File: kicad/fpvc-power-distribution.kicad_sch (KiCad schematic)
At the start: 0 parts

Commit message: feat: Plan mosfet based solenoid and clutch actuation
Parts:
- added D1, D2, D4: 1N5819, Diode_THT:D_DO-41_SOD81_P10.16mm_Horizontal, symbol Diode:1N5819
- added J1, J3: Solenoid1, symbol Connector:Screw_Terminal_01x02
- added J2: PLC-S1, symbol Connector:Screw_Terminal_01x01
- added J4: PLC-S2, symbol Connector:Screw_Terminal_01x01
- added J6: Clutch, symbol Connector:Screw_Terminal_01x02
- added J8: PLC-C, symbol Connector:Screw_Terminal_01x01
- added Q1, Q2, Q4: IRLZ44N, Package_TO_SOT_THT:TO-220-3_Vertical, symbol Transistor_FET:IRLZ44N
- added R1, R3, R6: 220, symbol Device:R
- added R2, R4, R8: 10k, symbol Device:R
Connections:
- new net: D2.1 (K), J3.1 (Pin_1)
- new net: D2.2 (A), J3.2 (Pin_2), Q2.2 (D)
- new net: J2.1 (Pin_1), R1.1
- new net: Q1.1 (G), R1.2, R2.1
- new net: J8.1 (Pin_1), R6.1
- new net: Q4.1 (G), R6.2, R8.1
- new net: D4.2 (A), J6.2 (Pin_2), Q4.2 (D)
- new net: D1.1 (K), J1.1 (Pin_1)
- new net: D1.2 (A), J1.2 (Pin_2), Q1.2 (D)
- new net: Q2.1 (G), R3.2, R4.1
- new net: J4.1 (Pin_1), R3.1
- new net +12V: D4.1 (K), J6.1 (Pin_1)
- new net GND: Q1.3 (S), Q2.3 (S), Q4.3 (S), R2.2, R4.2, R8.2
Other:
- company: (none) -> Aiden Cherniske | Bucknell Mechanical Engineering Department
- title: (none) -> Fluid Power Vehicle Challenge Power Distribution Board

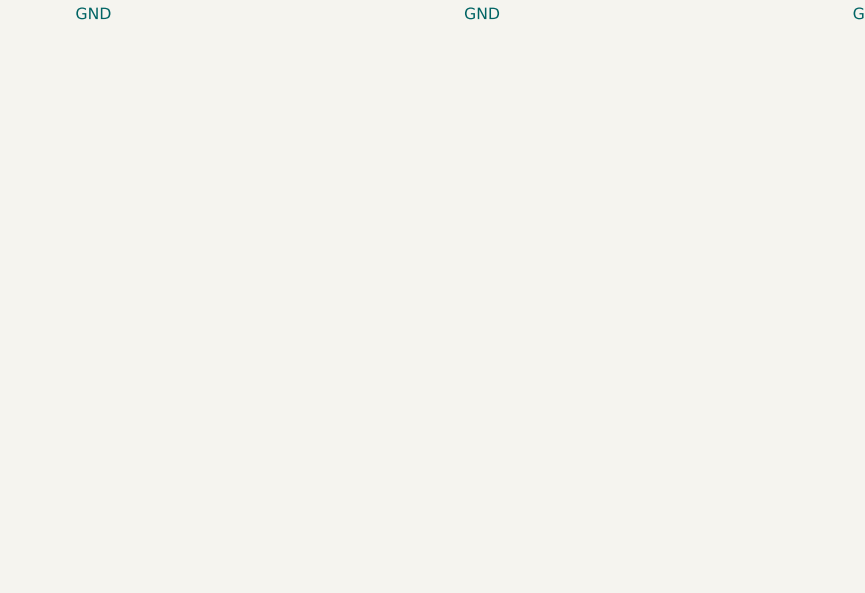
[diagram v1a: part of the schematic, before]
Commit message: feat: Create voltage regulator symbol and schematic
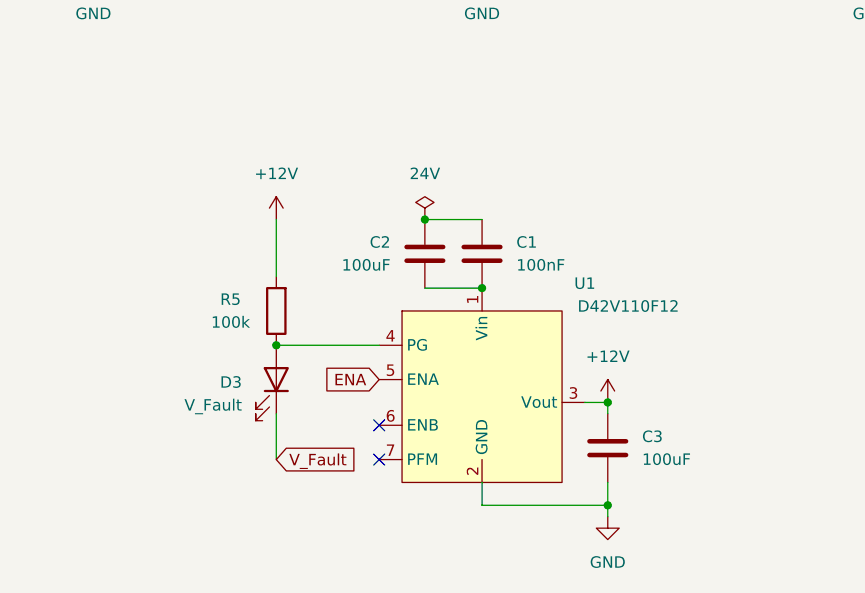
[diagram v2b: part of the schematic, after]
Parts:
- added C1: 100nF, symbol Device:C
- added C2, C3: 100uF, symbol Device:C
- added D3: V_Fault, symbol Device:LED
- added R5: 100k, symbol Device:R
- added U1: D42V110F12, symbol library:D42V110F12
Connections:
- net +12V: now also C3.1, R5.2, U1.3 (Vout)
- net GND: now also C3.2, U1.2 (GND)
- new net: D3.2 (A), R5.1, U1.4 (PG)
- new net: C1.2, C2.2, U1.1 (Vin)
- new net: C1.1, C2.1
- new net ENA: U1.5 (ENA)
- new net V_Fault: D3.1 (K)
- no-connect marks 0 -> 2

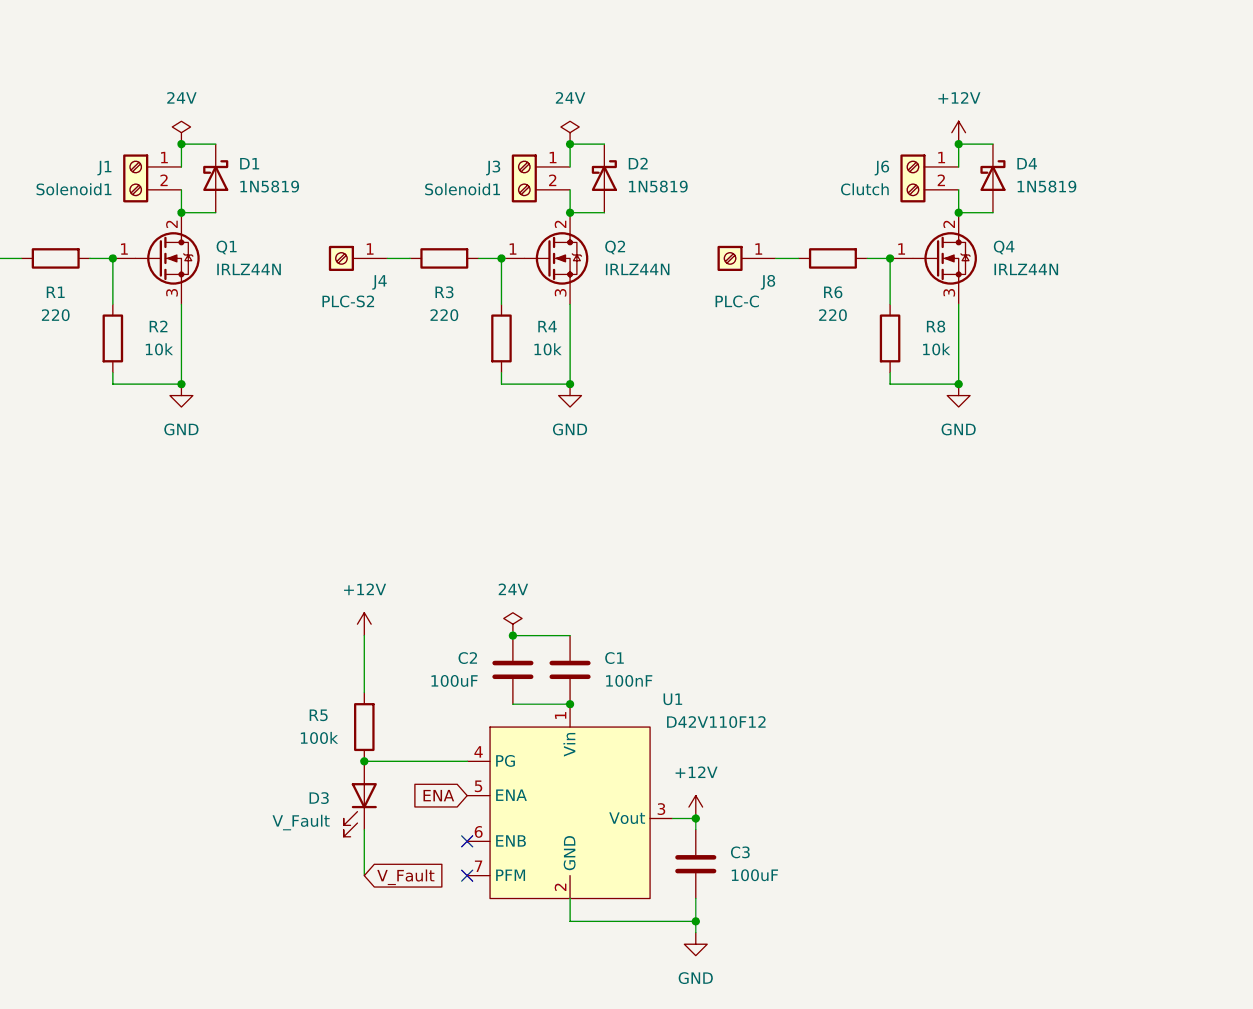
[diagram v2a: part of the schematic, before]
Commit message: feat: Add proper regulator fault detection and power indication
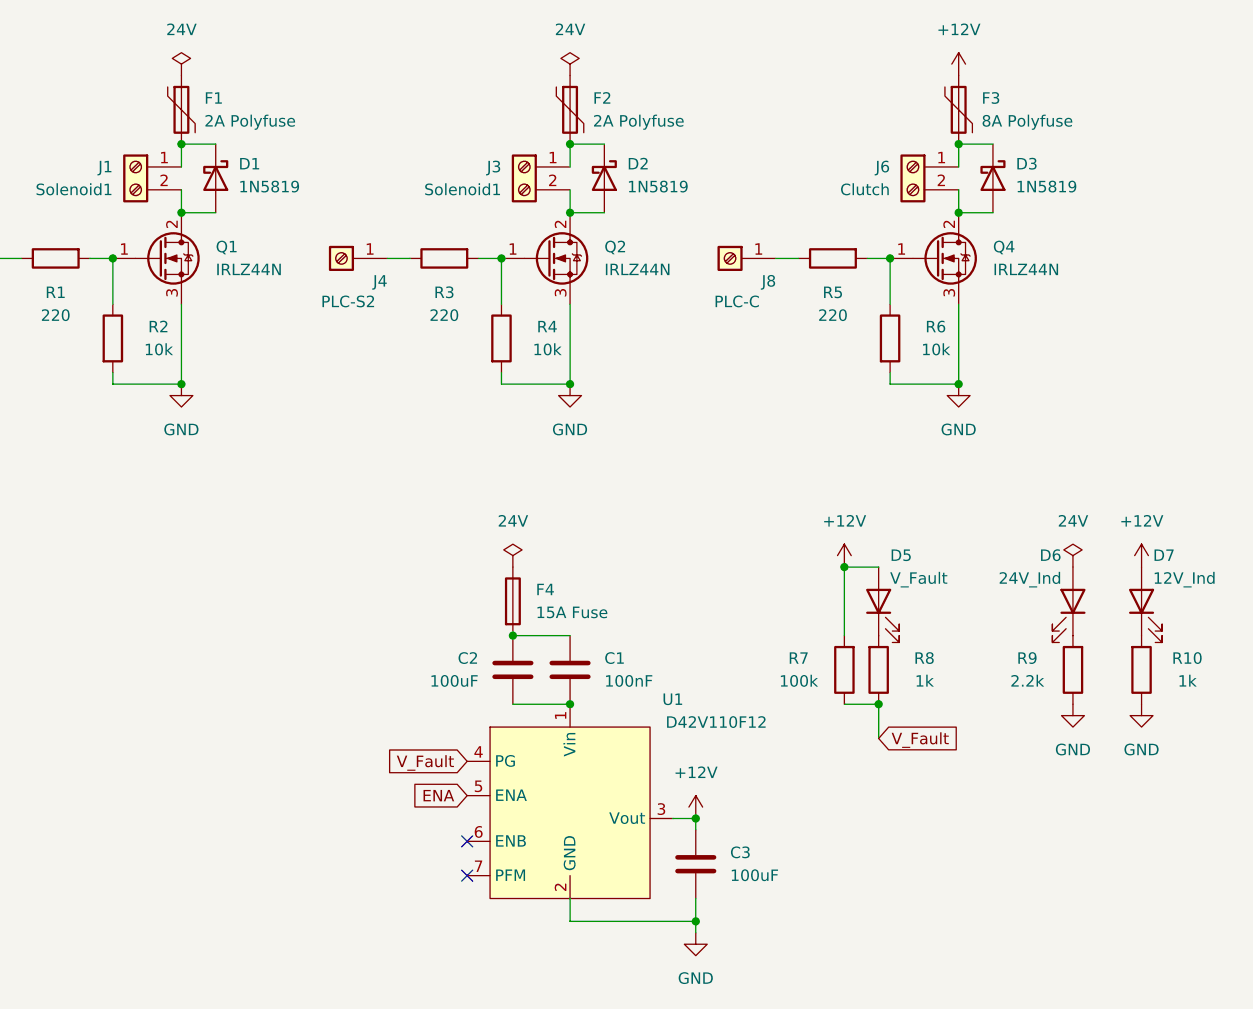
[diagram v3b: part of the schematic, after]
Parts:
- removed D3: V_Fault, symbol Device:LED
- added D5: V_Fault, symbol Device:LED
- added D6: 24V_Ind, symbol Device:LED
- added D7: 12V_Ind, symbol Device:LED
- added F1, F2: 2A Polyfuse, symbol Device:Polyfuse
- added F3: 8A Polyfuse, symbol Device:Polyfuse
- added F4: 15A Fuse, symbol Device:Fuse
- added R10, R8: 1k, symbol Device:R
- added R9: 2.2k, symbol Device:R
- renumbered D4 to D3, R6 to R5, R8 to R6, R5 to R7
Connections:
- net +12V: now also D5.2 (A), D7.2 (A), F3.1; no longer D3.1 (K), J6.1 (Pin_1)
- net GND: now also R10.1, R9.1
- net V_Fault: now also R7.1, U1.4 (PG), R8.1
- net at D2.1 (K), J3.1 (Pin_1): now also F2.2
- net at D1.1 (K), J1.1 (Pin_1): now also F1.2
- net at C1.1, C2.1: now also F4.2
- new net: D6.1 (K), R9.2
- new net: D7.1 (K), R10.2
- new net: D5.1 (K), R8.2
- new net: D3.1 (K), F3.2, J6.1 (Pin_1)
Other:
- moved on the sheet: R7

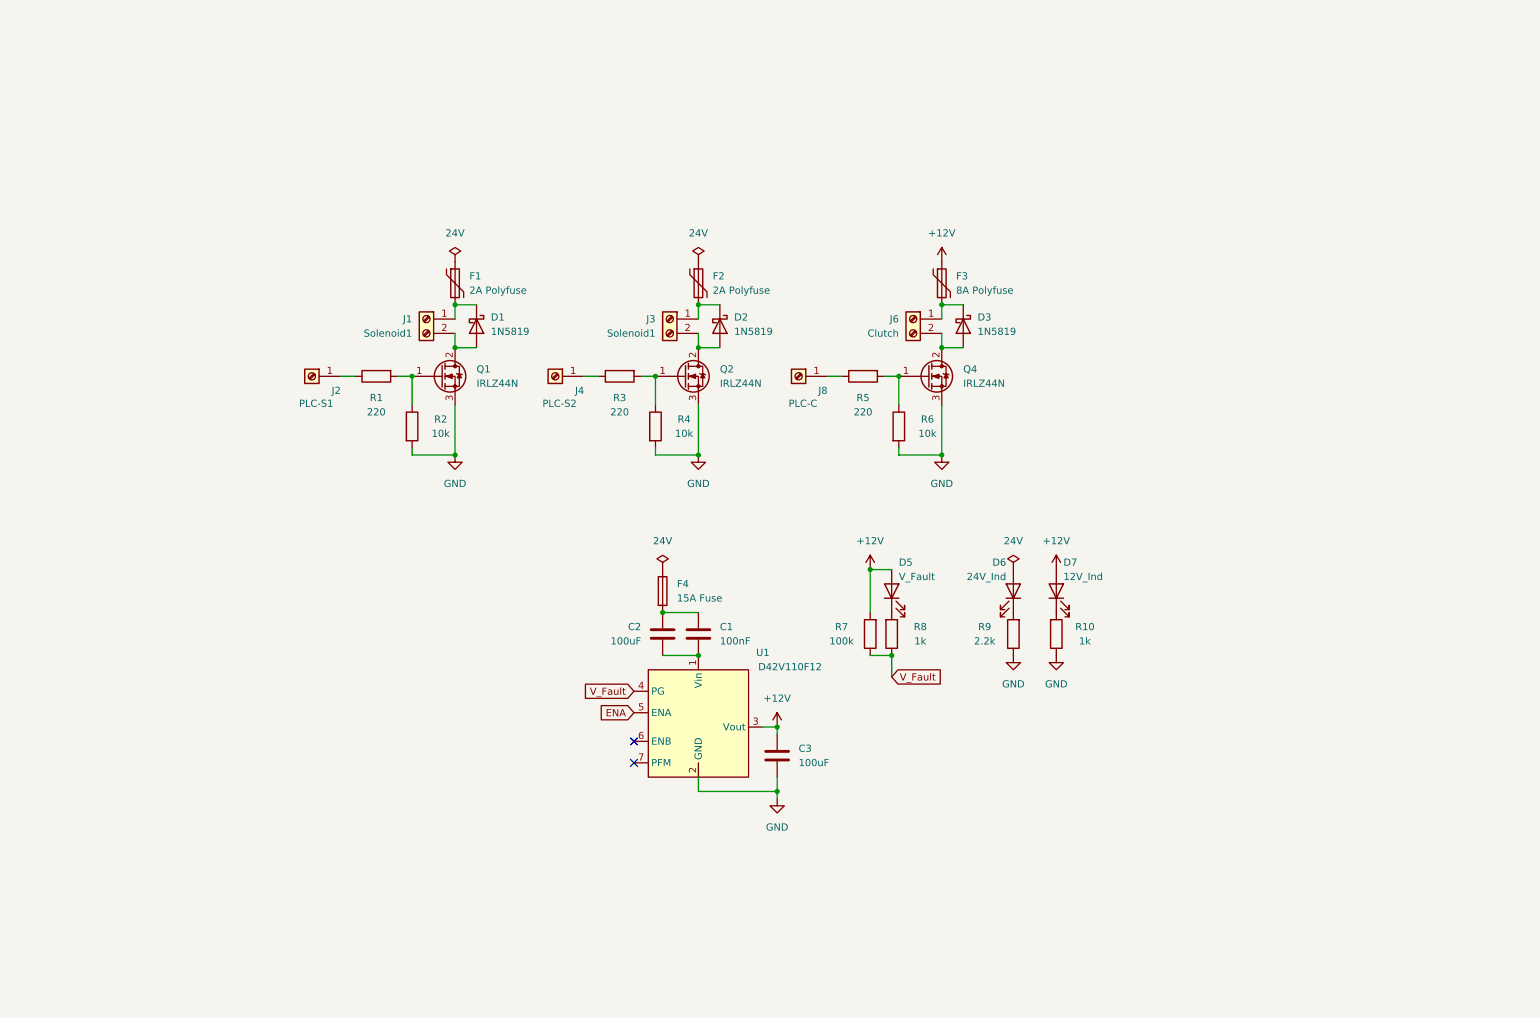
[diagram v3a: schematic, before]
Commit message: feat: Add 5V DC/DC converter for PLC
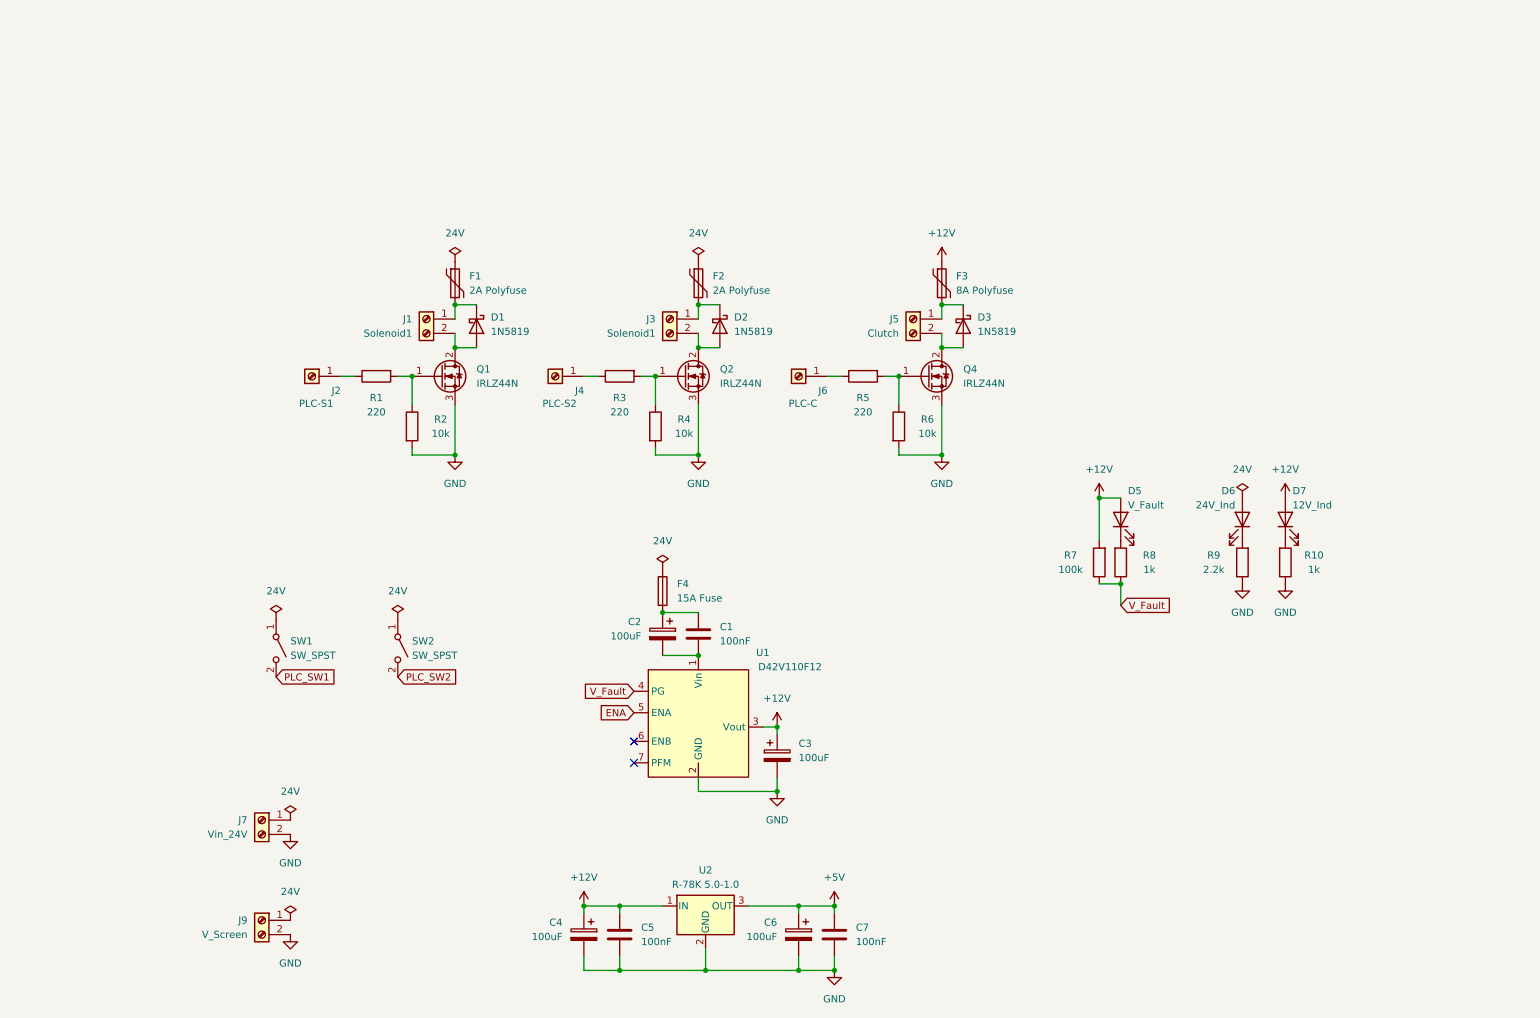
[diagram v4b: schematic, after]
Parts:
- removed C2, C3: 100uF, symbol Device:C
- added C2, C3, C4, C6: 100uF, symbol Device:C_Polarized
- added C5, C7: 100nF, symbol Device:C
- added J7: Vin_24V, symbol Connector:Screw_Terminal_01x02
- added J9: V_Screen, symbol Connector:Screw_Terminal_01x02
- added SW1, SW2: SW_SPST, symbol Switch:SW_SPST
- added U2: R-78K 5.0-1.0, Converter_DCDC:Converter_DCDC_RECOM_R-78E-0.5_THT, symbol Regulator_Switching:R-785.0-1.0
- renumbered J6 to J5, J8 to J6
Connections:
- net +12V: now also C3.1, C4.1, C5.1, U2.1 (IN)
- net GND: now also C3.2, C4.2, C5.2, C6.2, C7.2, J7.2 (Pin_2), J9.2 (Pin_2), U2.2 (GND)
- net at C1.1, F4.2: now also C2.1
- net at C1.2, U1.1 (Vin): now also C2.2
- new net +5V: C6.1, C7.1, U2.3 (OUT)
- new net PLC_SW1: SW1.2 (B)
- new net PLC_SW2: SW2.2 (B)
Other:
- moved on the sheet: D5, D6, D7, R10, R7, R8, R9

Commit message: style: Clean up schematic and add labels
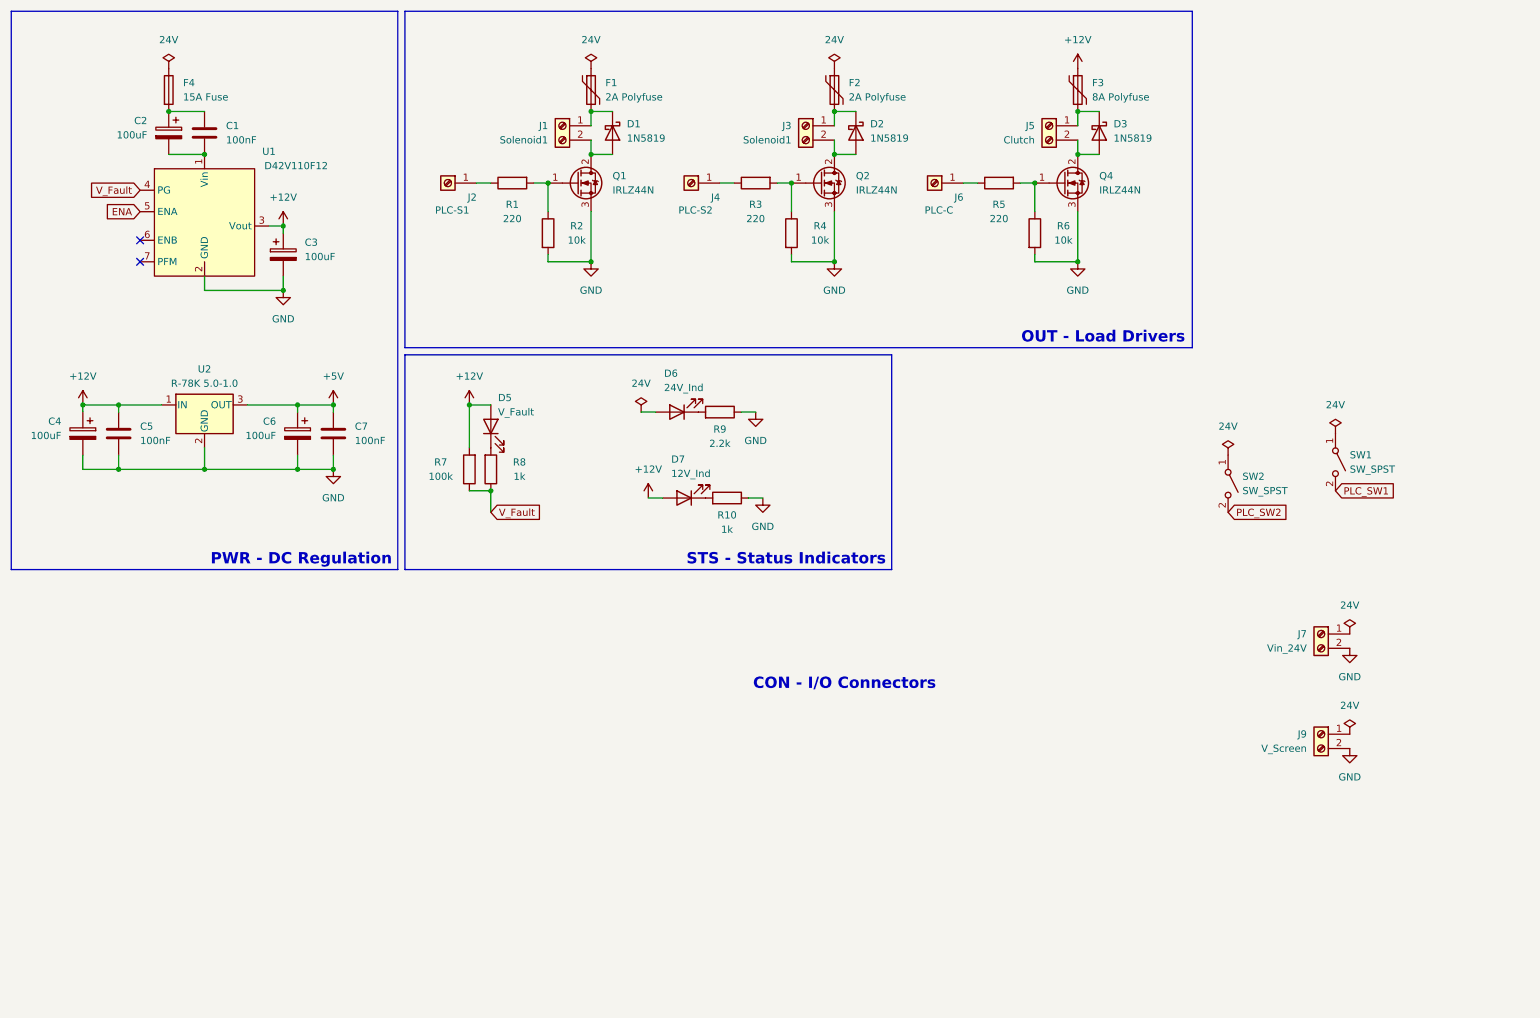
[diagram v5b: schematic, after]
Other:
- note added: "CON - I/O Connectors"
- note added: "OUT - Load Drivers"
- note added: "PWR - DC Regulation"
- note added: "STS - Status Indicators"
- moved on the sheet: C1, C2, C3, C4, C5, C6, C7, D1, D2, D3, D5, D7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

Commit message: style: Complete schematic formatting
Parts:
- added J8: V_PLC, symbol Connector:Screw_Terminal_01x02
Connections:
- net +5V: now also J8.1 (Pin_1)
- net GND: now also J8.2 (Pin_2)
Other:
- moved on the sheet: C1, C2, C3, C4, C5, C6, C7, D1, D2, D3, D5, D6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
